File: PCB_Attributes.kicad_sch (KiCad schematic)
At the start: 5 parts

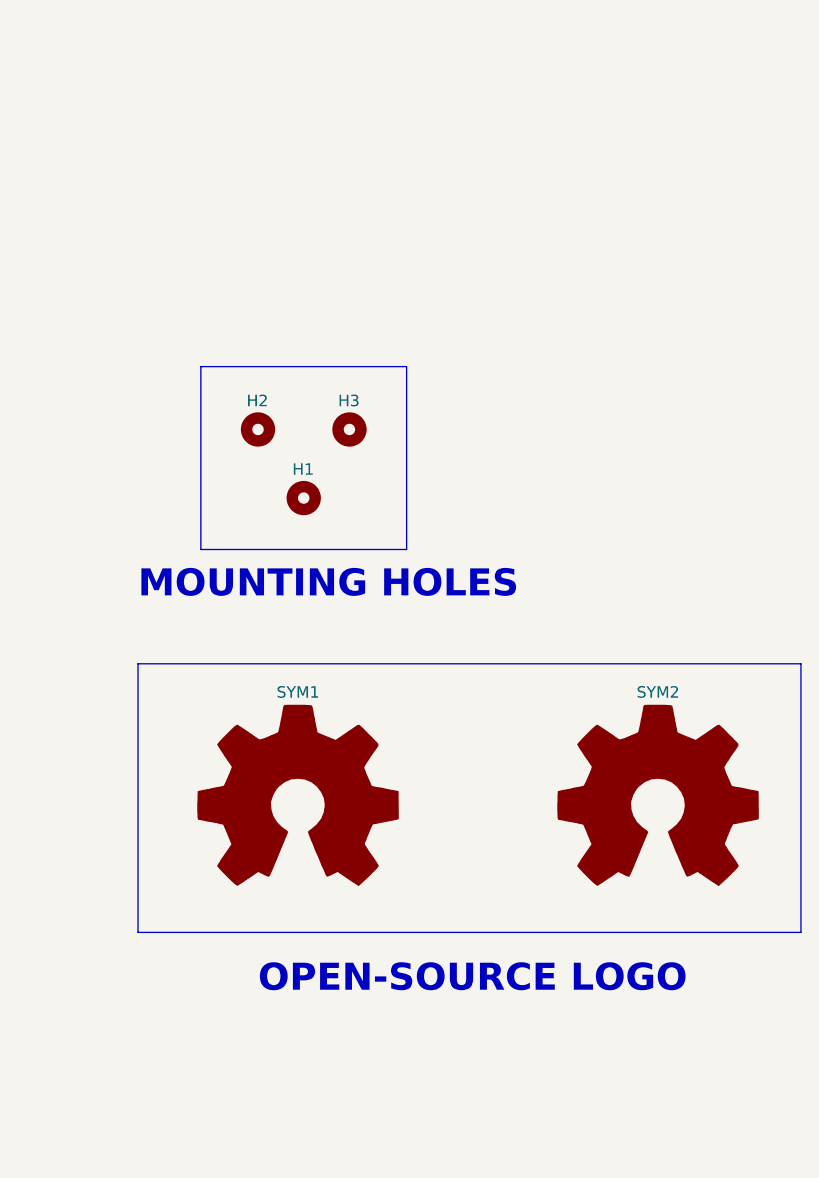
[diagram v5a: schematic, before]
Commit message: Added Arduino style SS for GPIO headers, Added BLE & Wi-Fi symbol
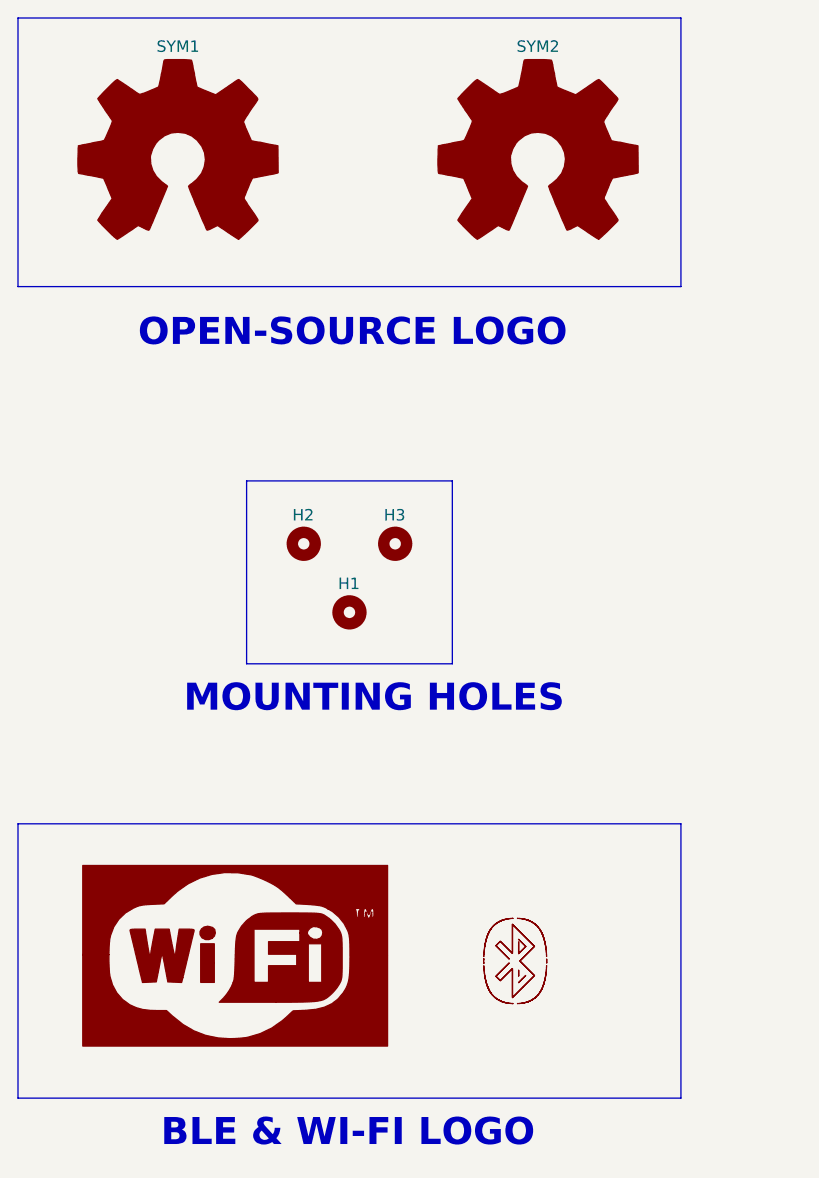
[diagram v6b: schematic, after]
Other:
- note added: "BLE & WI-FI LOGO"
- moved on the sheet: H1, H2, H3, SYM1, SYM2
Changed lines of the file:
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@@
 (kicad_sch (version 20230121) (generator eeschema)
   (paper "A4")
-  (bus (pts (xy 130.175 106.045) (xy 203.835 106.045))
-    (stroke (width 1) (type default) (color 72 72 72 1))
-  )
-  (bus (pts (xy 130.175 135.89) (xy 130.175 106.045))
-    (stroke (width 1) (type default) (color 72 72 72 1))
-  )
-  (bus (pts (xy 203.835 106.045) (xy 203.835 135.89))
-    (stroke (width 1) (type default) (color 72 72 72 1))
-  )
-  (bus (pts (xy 130.175 135.89) (xy 203.835 135.89))
-    (stroke (width 1) (type default) (color 72 72 72 1))
-  )
-  (bus (pts (xy 137.16 93.345) (xy 137.16 73.025))
-    (stroke (width 1) (type default) (color 72 72 72 1))
-  )
-  (bus (pts (xy 137.16 93.345) (xy 160.02 93.345))
-    (stroke (width 1) (type default) (color 72 72 72 1))
-  )
-  (bus (pts (xy 137.16 73.025) (xy 160.02 73.025))
-    (stroke (width 1) (type default) (color 72 72 72 1))
-  )
-  (bus (pts (xy 160.02 73.025) (xy 160.02 93.345))
-    (stroke (width 1) (type default) (color 72 72 72 1))
-  )
-  (text "OPEN-SOURCE LOGO" (at 143.51 142.875 0)
+  (bus (pts (xy 116.84 34.29) (xy 190.5 34.29))
+    (stroke (width 1) (type default) (color 72 72 72 1))
+  )
+  (bus (pts (xy 116.84 64.135) (xy 116.84 34.29))
+    (stroke (width 1) (type default) (color 72 72 72 1))
+  )
+  (bus (pts (xy 190.5 34.29) (xy 190.5 64.135))
+    (stroke (width 1) (type default) (color 72 72 72 1))
+  )
+  (bus (pts (xy 116.84 154.305) (xy 116.84 123.825))
+    (stroke (width 1) (type default) (color 72 72 72 1))
+  )
+  (bus (pts (xy 116.84 123.825) (xy 190.5 123.825))
+    (stroke (width 1) (type default) (color 72 72 72 1))
+  )
+  (bus (pts (xy 116.84 64.135) (xy 190.5 64.135))
+    (stroke (width 1) (type default) (color 72 72 72 1))
+  )
+  (bus (pts (xy 142.24 106.045) (xy 142.24 85.725))
+    (stroke (width 1) (type default) (color 72 72 72 1))
+  )
+  (bus (pts (xy 190.5 154.305) (xy 116.84 154.305))
+    (stroke (width 1) (type default) (color 72 72 72 1))
+  )
+  (bus (pts (xy 142.24 106.045) (xy 165.1 106.045))
+    (stroke (width 1) (type default) (color 72 72 72 1))
+  )
+  (bus (pts (xy 142.24 85.725) (xy 165.1 85.725))
+    (stroke (width 1) (type default) (color 72 72 72 1))
+  )
+  (bus (pts (xy 190.5 123.825) (xy 190.5 154.305))
+    (stroke (width 1) (type default) (color 72 72 72 1))
+  )
+  (bus (pts (xy 165.1 85.725) (xy 165.1 106.045))
+    (stroke (width 1) (type default) (color 72 72 72 1))
+  )
+  (text "OPEN-SOURCE LOGO" (at 130.175 71.12 0)
     (effects (font (size 3 3) bold (color 255 0 0 1)) (justify left bottom))
   )
-  (text "MOUNTING HOLES" (at 130.175 99.06 0)
+  (text "BLE & WI-FI LOGO" (at 132.715 160.02 0)
     (effects (font (size 3 3) bold (color 255 0 0 1)) (justify left bottom))
   )
-  (symbol (lib_id "ESP32-S3_DB:MountingHole") (at 148.59 87.63 0) (unit 1)
+  (text "MOUNTING HOLES" (at 135.255 111.76 0)
+    (effects (font (size 3 3) bold (color 255 0 0 1)) (justify left bottom))
+  )
+  (symbol (lib_id "ESP32-S3_DB:MountingHole") (at 153.67 100.33 0) (unit 1)
     (in_bom yes) (on_board yes) (dnp no)
-    (property "Reference" "H1" (at 147.32 84.455 0)
+    (property "Reference" "H1" (at 152.4 97.155 0)
       (effects (font (size 1.27 1.27)) (justify left))
     )
-    (property "Value" "MountingHole" (at 151.13 88.9 0)
+    (property "Value" "MountingHole" (at 156.21 101.6 0)
       (effects (font (size 1.27 1.27)) (justify left) hide)
     )
-    (property "Footprint" "ESP32-S3_Dev_Board:MountingHole_3.2mm_M3" (at 148.59 87.63 0)
-      (effects (font (size 1.27 1.27)) hide)
-    )
-    (property "Datasheet" "~" (at 148.59 87.63 0)
+    (property "Footprint" "ESP32-S3_Dev_Board:MountingHole_3.2mm_M3" (at 153.67 100.33 0)
+      (effects (font (size 1.27 1.27)) hide)
+    )
+    (property "Datasheet" "~" (at 153.67 100.33 0)
       (effects (font (size 1.27 1.27)) hide)
     )
@@
     )
   )
-  (symbol (lib_id "ESP32-S3_DB:MountingHole") (at 153.67 80.01 0) (unit 1)
+  (symbol (lib_id "ESP32-S3_DB:MountingHole") (at 158.75 92.71 0) (unit 1)
     (in_bom yes) (on_board yes) (dnp no)
-    (property "Reference" "H3" (at 152.4 76.835 0)
+    (property "Reference" "H3" (at 157.48 89.535 0)
       (effects (font (size 1.27 1.27)) (justify left))
     )
-    (property "Value" "MountingHole" (at 156.21 81.28 0)
+    (property "Value" "MountingHole" (at 161.29 93.98 0)
       (effects (font (size 1.27 1.27)) (justify left) hide)
     )
-    (property "Footprint" "ESP32-S3_Dev_Board:MountingHole_3.2mm_M3" (at 153.67 80.01 0)
-      (effects (font (size 1.27 1.27)) hide)
-    )
-    (property "Datasheet" "~" (at 153.67 80.01 0)
+    (property "Footprint" "ESP32-S3_Dev_Board:MountingHole_3.2mm_M3" (at 158.75 92.71 0)
+      (effects (font (size 1.27 1.27)) hide)
+    )
+    (property "Datasheet" "~" (at 158.75 92.71 0)
       (effects (font (size 1.27 1.27)) hide)
     )
@@
     )
   )
-  (symbol (lib_id "ESP32-S3_DB:Logo_Open_Hardware_Large") (at 187.96 121.92 0) (unit 1)
+  (symbol (lib_id "ESP32-S3_DB:BLE_Logo") (at 172.085 139.065 0) (unit 1)
+    (in_bom yes) (on_board yes) (dnp no) (fields_autoplaced)
+    (property "Reference" "#G2" (at 172.085 134.9623 0)
+      (effects (font (size 1.27 1.27)) hide)
+    )
+    (property "Value" "BLE_Logo" (at 172.085 143.1677 0)
+      (effects (font (size 1.27 1.27)) hide)
+    )
+    (property "Footprint" "" (at 172.085 139.065 0)
+      (effects (font (size 1.27 1.27)) hide)
+    )
+    (property "Datasheet" "" (at 172.085 139.065 0)
+      (effects (font (size 1.27 1.27)) hide)
+    )
+    (instances
+      (project "ESP32-S3_DB"
+        (path "/b7fc4bd3-c219-4455-832b-8d795385dcf1/7ada9602-7e0d-4ea4-a634-9a5d8155ae8b"
+          (reference "#G2") (unit 1)
+        )
+      )
+    )
+  )
+  (symbol (lib_id "ESP32-S3_DB:WI-FI") (at 140.97 138.43 0) (unit 1)
     (in_bom no) (on_board no) (dnp no) (fields_autoplaced)
-    (property "Reference" "SYM2" (at 187.96 109.22 0)
+    (property "Reference" "#G1" (at 140.97 129.0906 0)
+      (effects (font (size 1.27 1.27)) hide)
+    )
+    (property "Value" "WI-FI" (at 140.97 147.7694 0)
+      (effects (font (size 1.27 1.27)) hide)
+    )
+    (property "Footprint" "ESP32-S3_Dev_Board:wifi" (at 140.97 138.43 0)
+      (effects (font (size 1.27 1.27)) hide)
+    )
+    (property "Datasheet" "" (at 140.97 138.43 0)
+      (effects (font (size 1.27 1.27)) hide)
+    )
+    (instances
+      (project "ESP32-S3_DB"
+        (path "/b7fc4bd3-c219-4455-832b-8d795385dcf1/7ada9602-7e0d-4ea4-a634-9a5d8155ae8b"
+          (reference "#G1") (unit 1)
+        )
+      )
+    )
+  )
+  (symbol (lib_id "ESP32-S3_DB:Logo_Open_Hardware_Large") (at 174.625 50.165 0) (unit 1)
+    (in_bom no) (on_board no) (dnp no) (fields_autoplaced)
+    (property "Reference" "SYM2" (at 174.625 37.465 0)
       (effects (font (size 1.27 1.27)))
     )
-    (property "Value" "Logo_Open_Hardware_Large" (at 187.96 132.08 0)
-      (effects (font (size 1.27 1.27)) hide)
-    )
-    (property "Footprint" "ESP32-S3_Dev_Board:OSHW-Symbol_6.7x6mm_Copper" (at 187.96 121.92 0)
-      (effects (font (size 1.27 1.27)) hide)
-    )
-    (property "Datasheet" "~" (at 187.96 121.92 0)
+    (property "Value" "Logo_Open_Hardware_Large" (at 174.625 60.325 0)
+      (effects (font (size 1.27 1.27)) hide)
+    )
+    (property "Footprint" "ESP32-S3_Dev_Board:OSHW-Symbol_6.7x6mm_Copper" (at 174.625 50.165 0)
+      (effects (font (size 1.27 1.27)) hide)
+    )
+    (property "Datasheet" "~" (at 174.625 50.165 0)
       (effects (font (size 1.27 1.27)) hide)
     )
@@
     )
   )
-  (symbol (lib_id "ESP32-S3_DB:Logo_Open_Hardware_Large") (at 147.955 121.92 0) (unit 1)
+  (symbol (lib_id "ESP32-S3_DB:Logo_Open_Hardware_Large") (at 134.62 50.165 0) (unit 1)
     (in_bom no) (on_board no) (dnp no) (fields_autoplaced)
-    (property "Reference" "SYM1" (at 147.955 109.22 0)
+    (property "Reference" "SYM1" (at 134.62 37.465 0)
       (effects (font (size 1.27 1.27)))
     )
-    (property "Value" "Logo_Open_Hardware_Large" (at 147.955 132.08 0)
-      (effects (font (size 1.27 1.27)) hide)
-    )
-    (property "Footprint" "ESP32-S3_Dev_Board:OSHW-Symbol_6.7x6mm_Copper" (at 147.955 121.92 0)
-      (effects (font (size 1.27 1.27)) hide)
-    )
-    (property "Datasheet" "~" (at 147.955 121.92 0)
+    (property "Value" "Logo_Open_Hardware_Large" (at 134.62 60.325 0)
+      (effects (font (size 1.27 1.27)) hide)
+    )
+    (property "Footprint" "ESP32-S3_Dev_Board:OSHW-Symbol_6.7x6mm_Copper" (at 134.62 50.165 0)
+      (effects (font (size 1.27 1.27)) hide)
+    )
+    (property "Datasheet" "~" (at 134.62 50.165 0)
       (effects (font (size 1.27 1.27)) hide)
     )
@@
     )
   )
-  (symbol (lib_id "ESP32-S3_DB:MountingHole") (at 143.51 80.01 0) (unit 1)
+  (symbol (lib_id "ESP32-S3_DB:MountingHole") (at 148.59 92.71 0) (unit 1)
     (in_bom yes) (on_board yes) (dnp no)
-    (property "Reference" "H2" (at 142.24 76.835 0)
+    (property "Reference" "H2" (at 147.32 89.535 0)
       (effects (font (size 1.27 1.27)) (justify left))
     )
-    (property "Value" "MountingHole" (at 146.05 81.28 0)
+    (property "Value" "MountingHole" (at 151.13 93.98 0)
       (effects (font (size 1.27 1.27)) (justify left) hide)
     )
-    (property "Footprint" "ESP32-S3_Dev_Board:MountingHole_3.2mm_M3" (at 143.51 80.01 0)
-      (effects (font (size 1.27 1.27)) hide)
-    )
-    (property "Datasheet" "~" (at 143.51 80.01 0)
-      (effects (font (size 1.27 1.27)) hide)
-    )
+    (property "Footprint" "ESP32-S3_Dev_Board:MountingHole_3.2mm_M3" (at 148.59 92.71 0)
+      (effects (font (size 1.27 1.27)) hide)
+    )
+    (property "Datasheet" "~" (at 148.59 92.71 0)
+      (effects (font (size 1.27 1.27)) hide)
+    )

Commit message: Updated Readme file
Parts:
- SYM1, SYM2: footprint ESP32-S3_Dev_Board:OSHW-Symbol_6.7x6mm_Copper -> ESP32-S3_Dev_Board:OSHW-Logo_11.4x12mm_SilkScreen
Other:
- moved on the sheet: H1, H2, H3, SYM1, SYM2

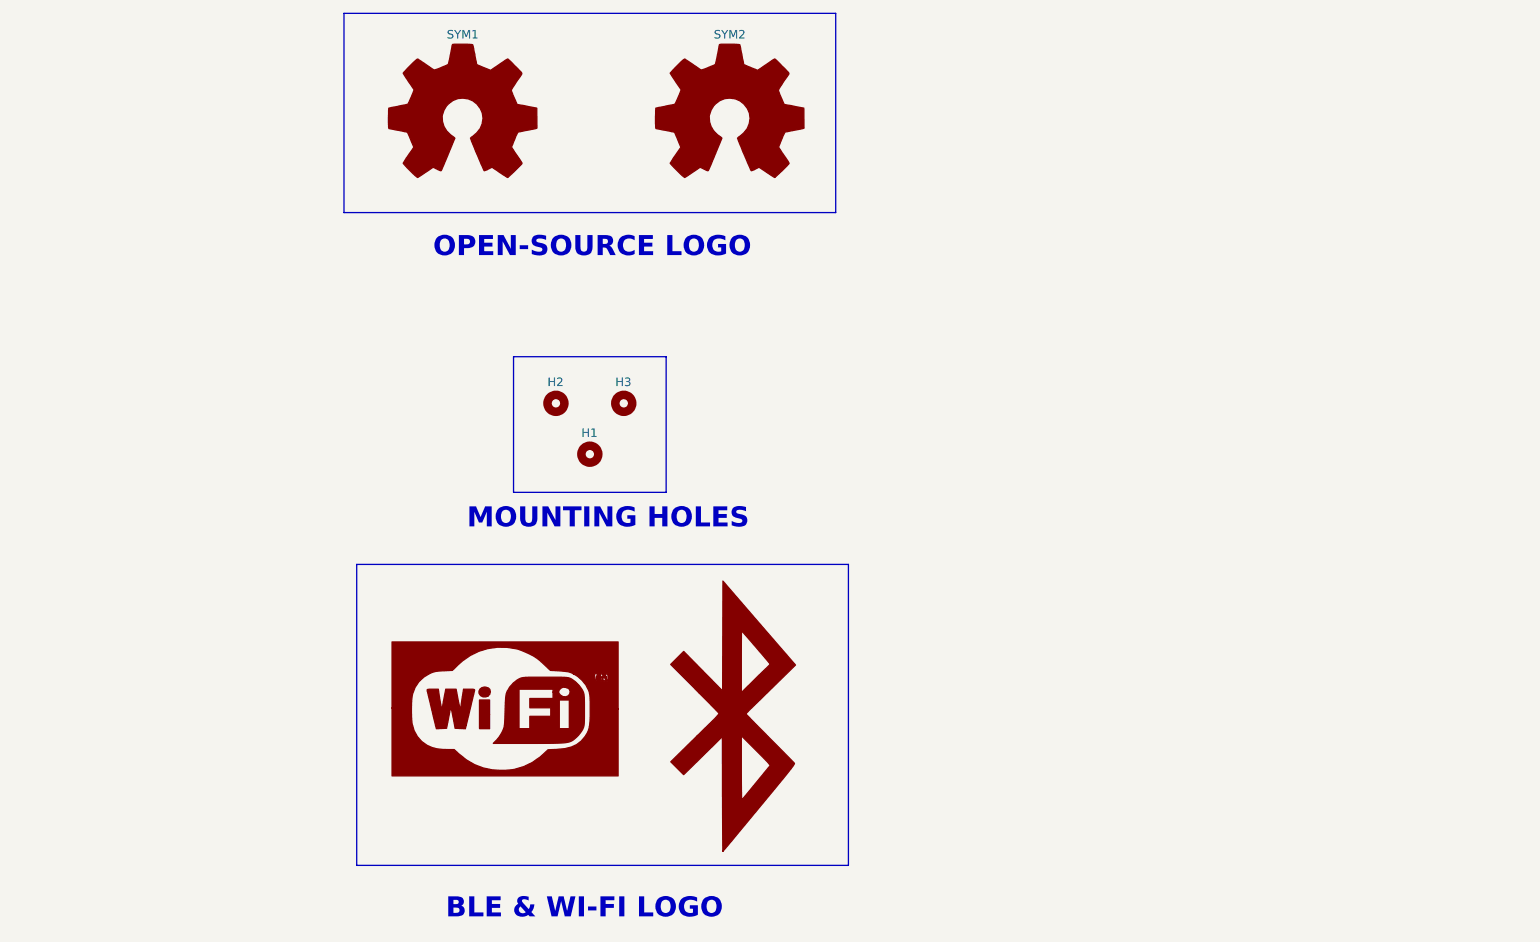
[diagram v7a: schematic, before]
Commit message: Added HW-Tinkerers logo and supporting graphics
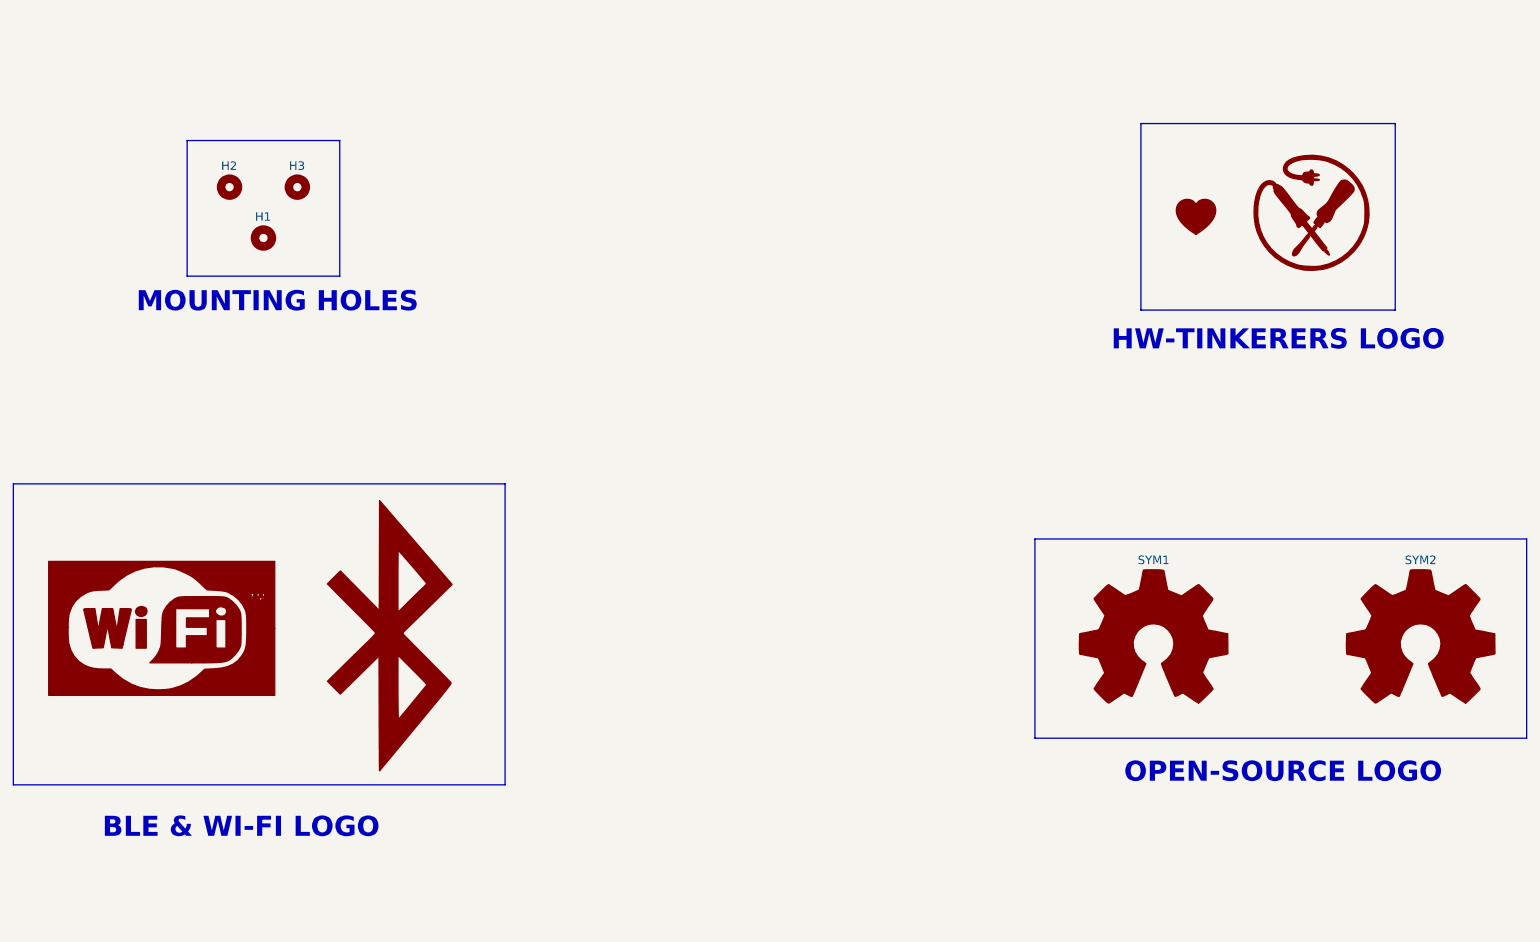
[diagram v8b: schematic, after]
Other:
- note added: "HW-TINKERERS LOGO"
- company: (none) -> HW-TINKERERS (hw.tinkerers@gmail.com)
- title: (none) -> HARDWARE TINKERERS ESP32-S3 DB
- moved on the sheet: H1, H2, H3, SYM1, SYM2
